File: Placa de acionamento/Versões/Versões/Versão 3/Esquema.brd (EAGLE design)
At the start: 68.6 x 45.8 mm, 22 parts, among them Q1 IRF540, Q2 IRF540

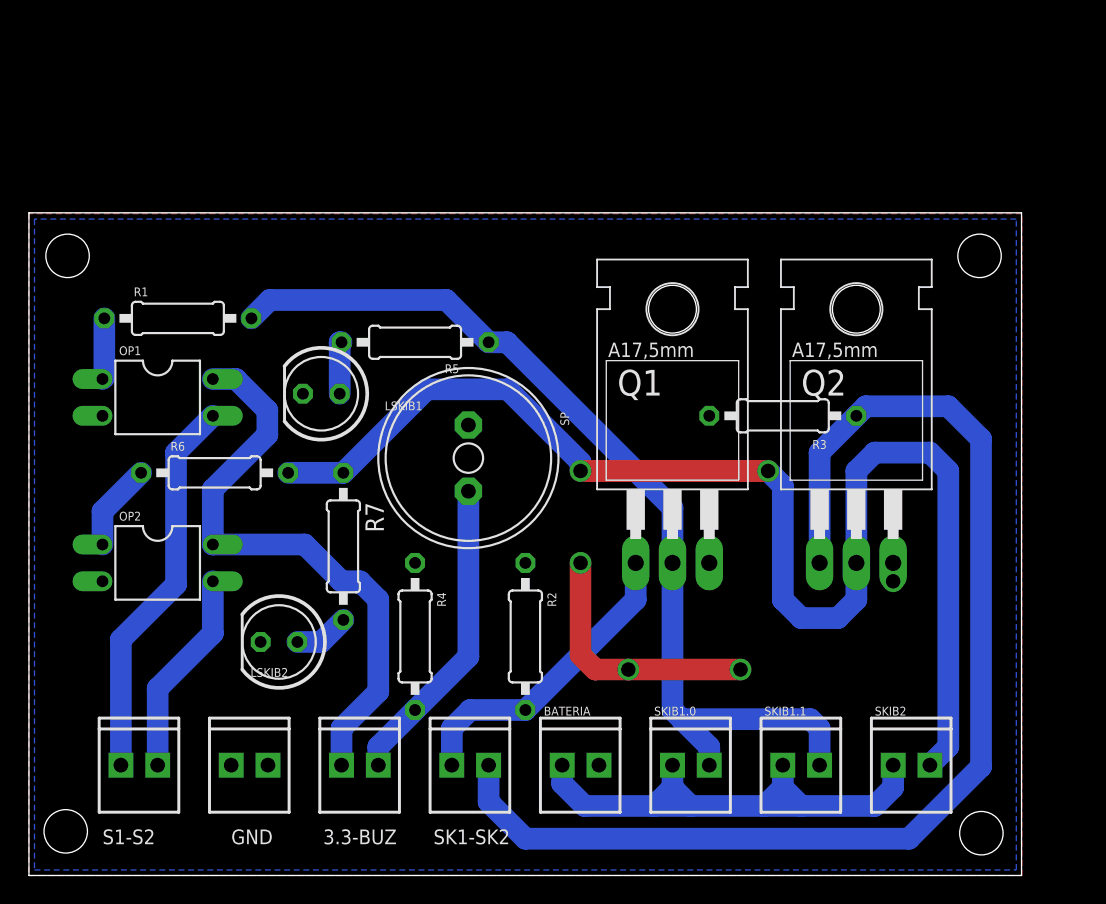
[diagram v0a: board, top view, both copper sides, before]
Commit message: CHORE: adicionando modelos 3D
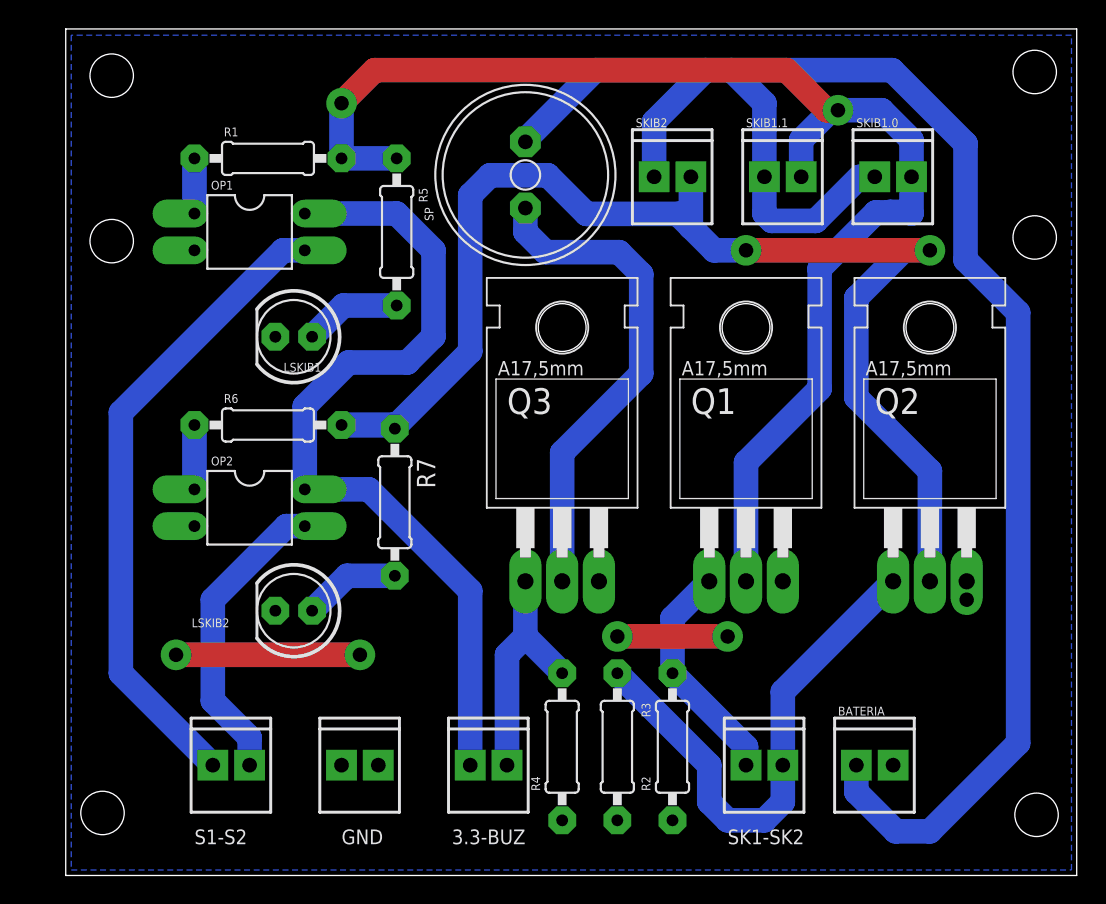
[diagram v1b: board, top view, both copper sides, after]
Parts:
- added Q3: IRF540, transistor-fet:TO220
- moved SKIB2 43.9 mm to (40.6, 48.3)
- moved SKIB1.0 43.0 mm to (55.9, 48.3)
- moved SKIB1.1 40.7 mm to (48.3, 48.3)
- moved R3 25.6 mm to (38.1, 8.89), turned to 90 degrees
- moved BATERIA 20.3 mm to (54.6, 7.62)
- moved SK1-SK2 20.3 mm to (47.0, 7.62)
- moved SP 20.0 mm to (31.8, 48.4), turned to 90 degrees
- moved OP1 13.1 mm to (12.7, 44.5)
- moved R4 12.7 mm to (34.3, 8.89), turned to 90 degrees
- moved R2 12.7 mm to (41.9, 8.89), turned to 90 degrees
- moved R1 12.7 mm to (14.0, 49.5)
- moved 3.3-BUZ 8.89 mm to (27.9, 7.62)
- moved R5 7.73 mm to (22.9, 44.5), turned to 270 degrees
- moved GND 7.62 mm to (19.1, 7.62)
- moved OP2 7.41 mm to (12.7, 25.4)
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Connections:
- new net N$2: Q3.2, SP.-
- net BUZZER: now also Q3.1; no longer SP.+
- net GND: now also Q3.3; no longer SP.-
- net VCC: now also SP.+
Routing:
- net VCC: track 37.1 -> 123.0 mm
- net SKIB2: track 83.3 -> 36.0 mm
- net N$2: track 0.00 -> 34.3 mm
- net SKIB1_CONECTOR: track 66.7 -> 92.7 mm, vias 0 -> 2
- net 3.3V: track 41.0 -> 58.9 mm
- net SINAL_SKIB1: track 26.8 -> 44.3 mm
- net SINAL_SKIB2: track 14.3 -> 20.9 mm
- net SKIB1: track 21.5 -> 15.9 mm
- net BUZZER: track 21.5 -> 16.8 mm
- net N$3: track 3.68 -> 6.74 mm
- net N$1: track 3.81 -> 6.71 mm
- net GND: track 17.8 -> 20.3 mm, vias 4 -> 5
- net N$5: track 6.06 -> 4.44 mm
- net SKIB2_CONECTOR: track 90.8 -> 91.8 mm
- removed copper zone on layer 1, net GND
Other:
- board size 68.6 x 45.8 mm -> 69.8 x 58.5 mm

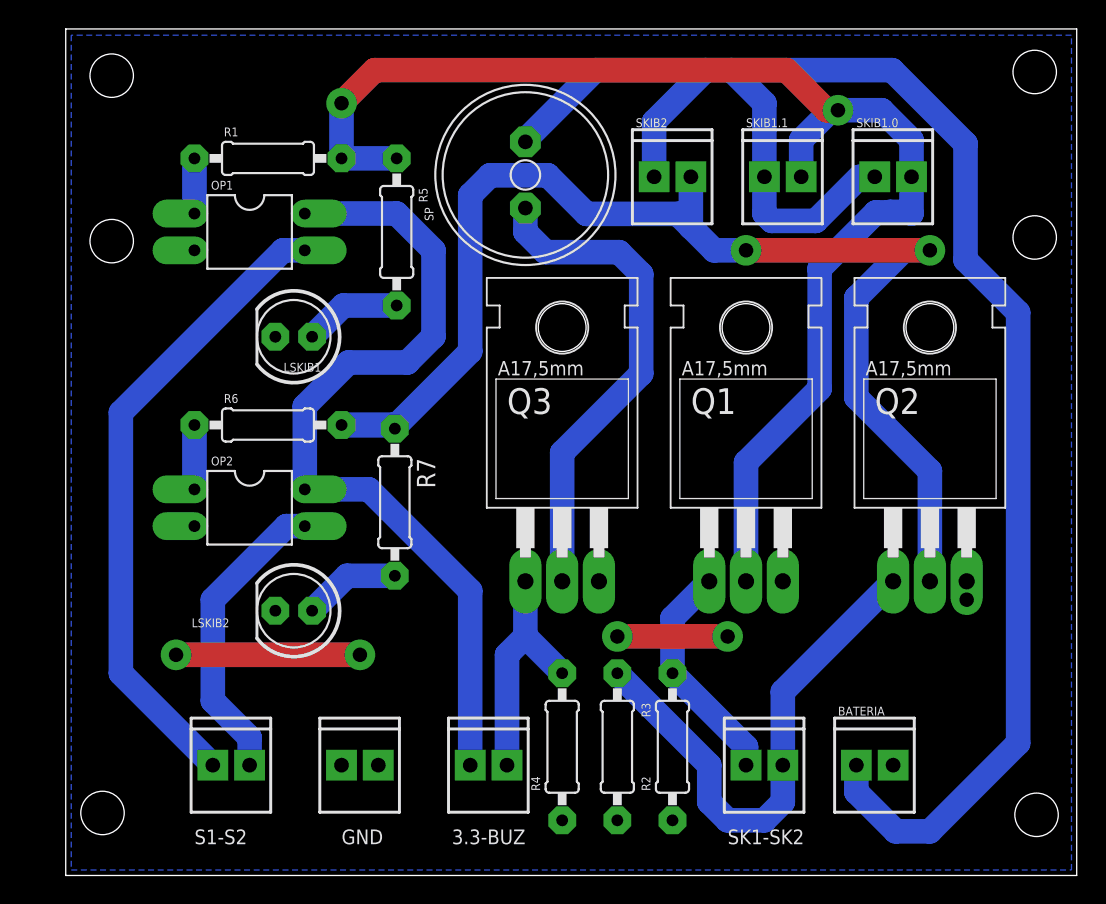
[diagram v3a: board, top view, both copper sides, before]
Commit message: CHORE: trocando conectores JST
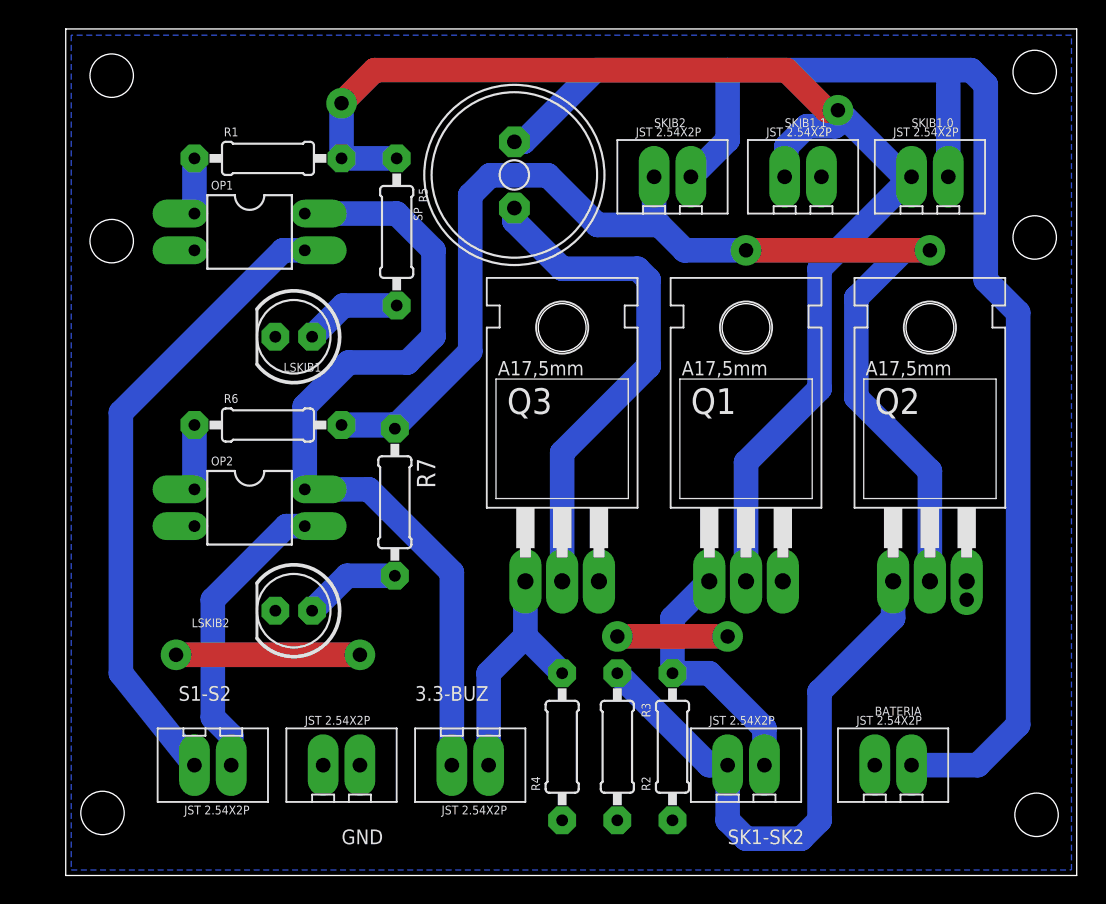
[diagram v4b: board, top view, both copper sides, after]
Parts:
- 3.3-BUZ, BATERIA, GND, S1-S2, SK1-SK2, SKIB1.0, SKIB1.1, SKIB2: value (none) -> JST2.54X2P; device SparkFun-Connectors:1X02_2.54_SCREWTERM -> CRD:JST2.54X2P_FOOTPRINT
- moved SKIB1.0 3.81 mm to (59.7, 48.3)
- moved SKIB1.1 2.67 mm to (50.9, 48.3)
- moved BATERIA 2.54 mm to (57.1, 7.62)
- moved SKIB2 1.27 mm to (41.9, 48.3)
- moved SP 0.76 mm to (31.0, 48.4)
- turned 3.3-BUZ to 180 degrees
- turned S1-S2 to 180 degrees
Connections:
- net 3.3V: now also 3.3-BUZ.2; no longer 3.3-BUZ.P2
- net BUZZER: now also 3.3-BUZ.1; no longer 3.3-BUZ.P1
- net GND: now also BATERIA.1, GND.1, GND.2; no longer BATERIA.P1, GND.P1, GND.P2
- net SINAL_SKIB1: now also S1-S2.2; no longer S1-S2.P2
- net SINAL_SKIB2: now also S1-S2.1; no longer S1-S2.P1
- net SKIB1: now also SK1-SK2.2; no longer SK1-SK2.P2
- net SKIB1_CONECTOR: now also SKIB1.0.1, SKIB1.1.1; no longer SKIB1.0.P1, SKIB1.1.P1
- net SKIB2: now also SK1-SK2.1; no longer SK1-SK2.P1
- net SKIB2_CONECTOR: now also SKIB2.1; no longer SKIB2.P1
- net VCC: now also BATERIA.2, SKIB1.0.2, SKIB1.1.2, SKIB2.2; no longer BATERIA.P2, SKIB1.0.P2, SKIB1.1.P2, SKIB2.P2
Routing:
- net VCC: track 123.0 -> 103.4 mm
- net SKIB2: track 36.0 -> 40.1 mm
- net SKIB1: track 15.9 -> 17.9 mm
- net SKIB1_CONECTOR: track 92.7 -> 90.9 mm
- net SINAL_SKIB1: track 44.3 -> 43.5 mm
- net N$2: track 34.3 -> 35.1 mm
- net SINAL_SKIB2: track 20.9 -> 20.4 mm
- net BUZZER: track 16.8 -> 17.3 mm
- net 3.3V: track 58.9 -> 58.4 mm

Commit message: CHORE: adicionando pads ovais
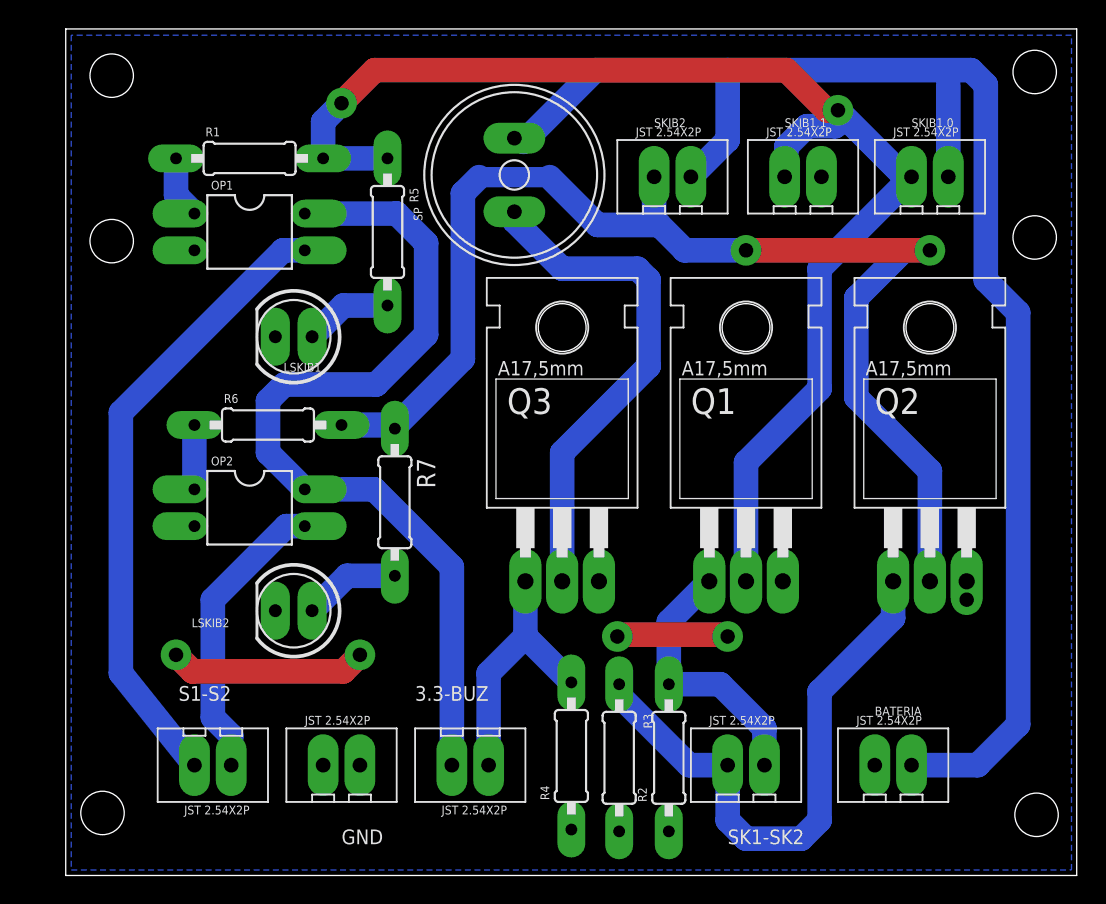
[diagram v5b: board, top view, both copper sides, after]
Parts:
- LSKIB1, LSKIB2: device led:LED5MM -> led-modificada:LED5MM
- R1, R2, R3, R4, R5, R6, R7: device rcl:0207/10 -> rcl-modificada:0207/10
- moved R1 1.27 mm to (12.7, 49.5)
- moved R4 0.90 mm to (34.9, 8.26)
- moved R2 0.80 mm to (41.7, 8.13)
- moved R3 0.77 mm to (38.2, 8.13)
- moved R5 0.63 mm to (22.2, 44.5)
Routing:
- net 3.3V: track 58.4 -> 61.6 mm
- net SKIB1_CONECTOR: track 90.9 -> 92.1 mm
- net GND: track 20.3 -> 21.4 mm
- net BUZZER: track 17.3 -> 18.2 mm
- net SKIB1: track 17.9 -> 18.7 mm
- net N$3: track 6.74 -> 6.10 mm
- net N$4: track 3.81 -> 4.34 mm

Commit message: placa de acionamento
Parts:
- moved SK1-SK2 1.98 mm to (48.5, 8.89)
- moved R4 1.65 mm to (33.3, 8.26)
- moved BATERIA 1.27 mm to (57.1, 8.89)
- moved R3 0.64 mm to (38.9, 8.13)
- moved SKIB1.1 0.25 mm to (50.7, 48.3), turned to 180 degrees
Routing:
- net VCC: track 103.5 -> 113.3 mm
- net SKIB2: track 40.1 -> 36.4 mm
- net 3.3V: track 61.6 -> 59.2 mm
- net BUZZER: track 18.2 -> 17.1 mm
- net N$2: track 34.9 -> 33.8 mm
- net SKIB1: track 18.7 -> 19.7 mm
- net SINAL_SKIB1: track 43.5 -> 42.9 mm
- net GND: vias 5 -> 4
